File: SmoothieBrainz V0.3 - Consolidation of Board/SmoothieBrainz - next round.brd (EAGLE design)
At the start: 101 x 101 mm, 213 parts, among them IC1 LPC1769, IC5 LD117ADT33TR, Q1 BSL207SP, Q2 12MHz, SW1 SW_TACT_4P_B, SW3 SW_TACT_4P_B, U3 USD-SOCKETUSD, X1 MSTBA2, X14 USBPTH, X2 GMSTBA2, X3 GMSTBA4, X4 1751248, X5 1751248, X6 1751248, X7 1751248

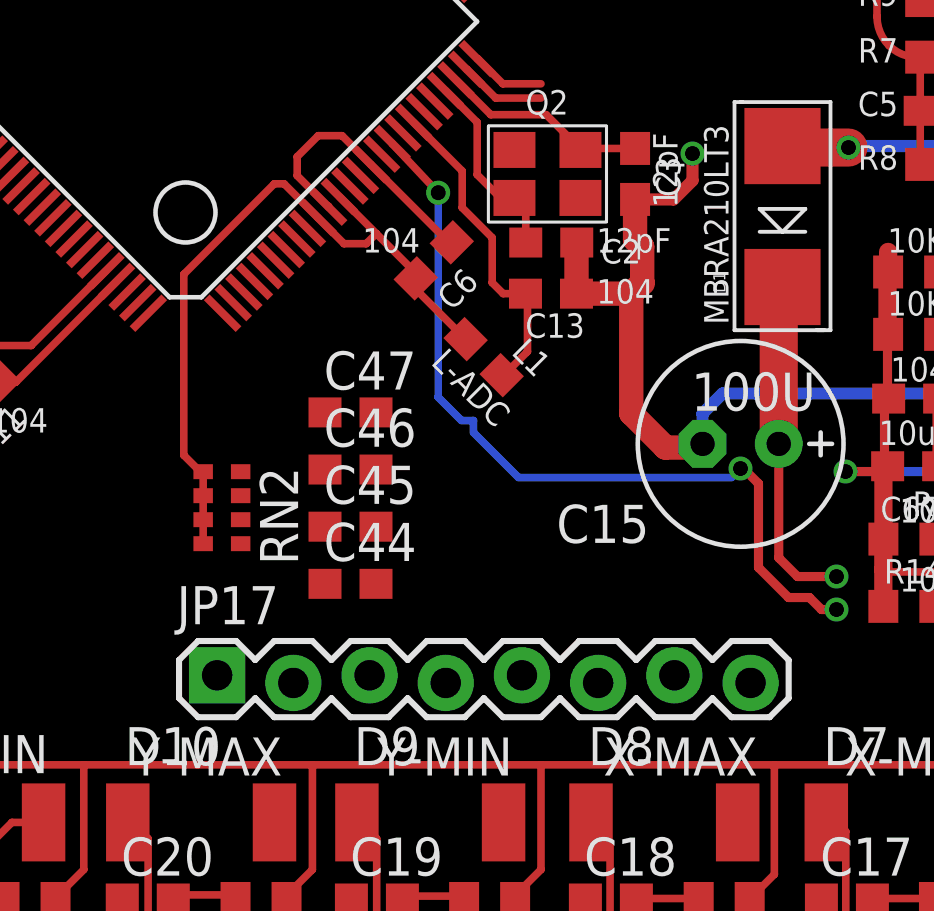
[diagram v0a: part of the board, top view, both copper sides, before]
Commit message: thermistor circuit, needs to be redone.  big time.
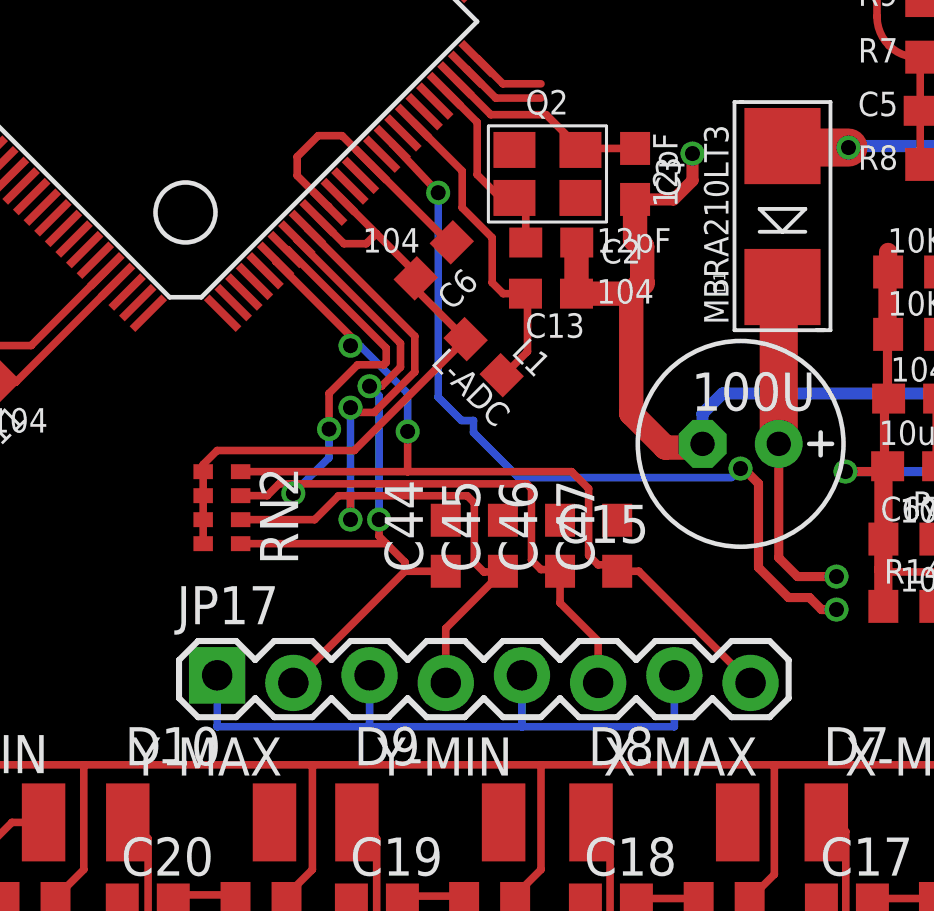
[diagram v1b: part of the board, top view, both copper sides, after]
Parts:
- moved C47 9.94 mm to (72.4, 18.4), turned to 90 degrees
- moved C46 7.43 mm to (70.5, 18.4), turned to 90 degrees
- moved C45 5.12 mm to (68.6, 18.4), turned to 90 degrees
- moved C44 3.42 mm to (66.7, 18.4), turned to 90 degrees
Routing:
- net TH4: track 0.00 -> 30.3 mm, vias 0 -> 2
- net TH1_HOTEND: track 0.00 -> 29.4 mm, vias 0 -> 2
- net TH3: track 0.00 -> 29.3 mm, vias 0 -> 2
- net TH2_BED: track 0.00 -> 25.1 mm, vias 0 -> 2
- net AGND: track 9.07 -> 31.2 mm
- net AVCC: track 26.0 -> 23.7 mm

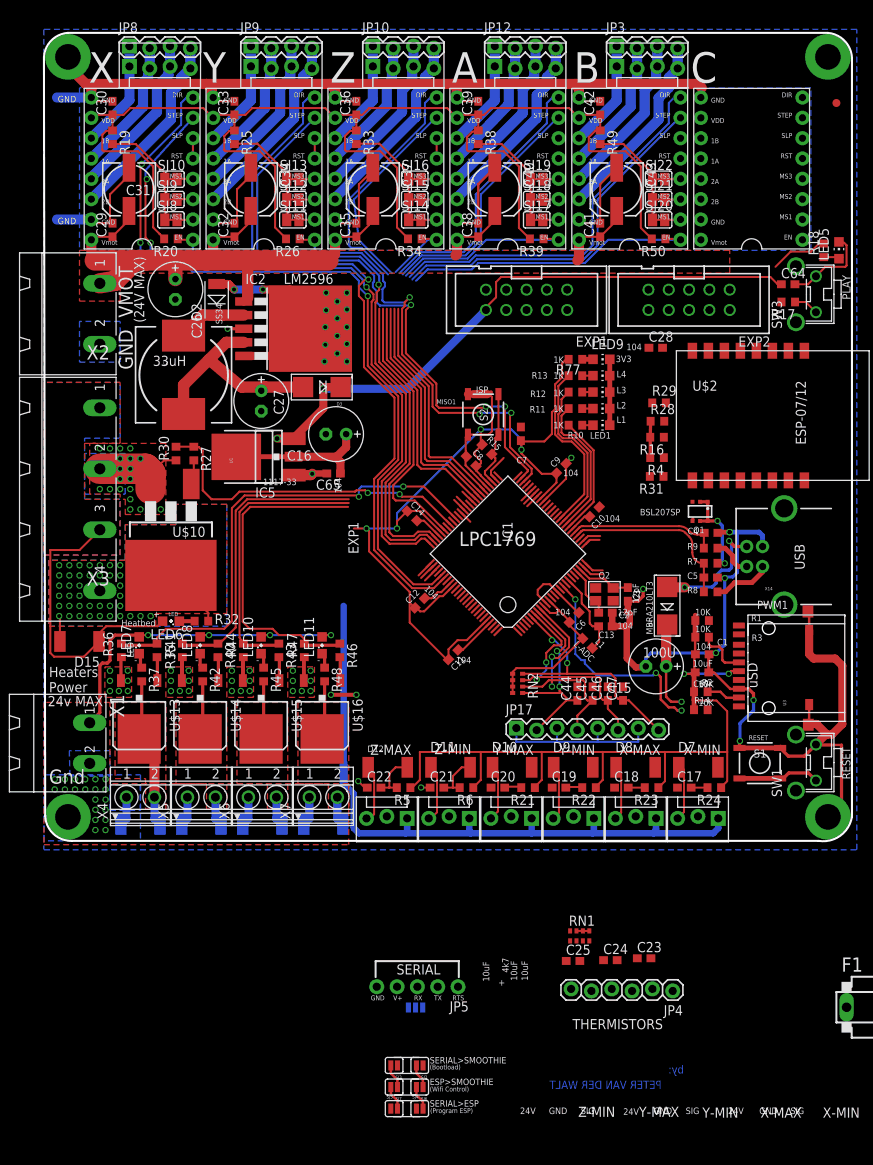
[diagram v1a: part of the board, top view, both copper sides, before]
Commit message: endstop power routing variant 1
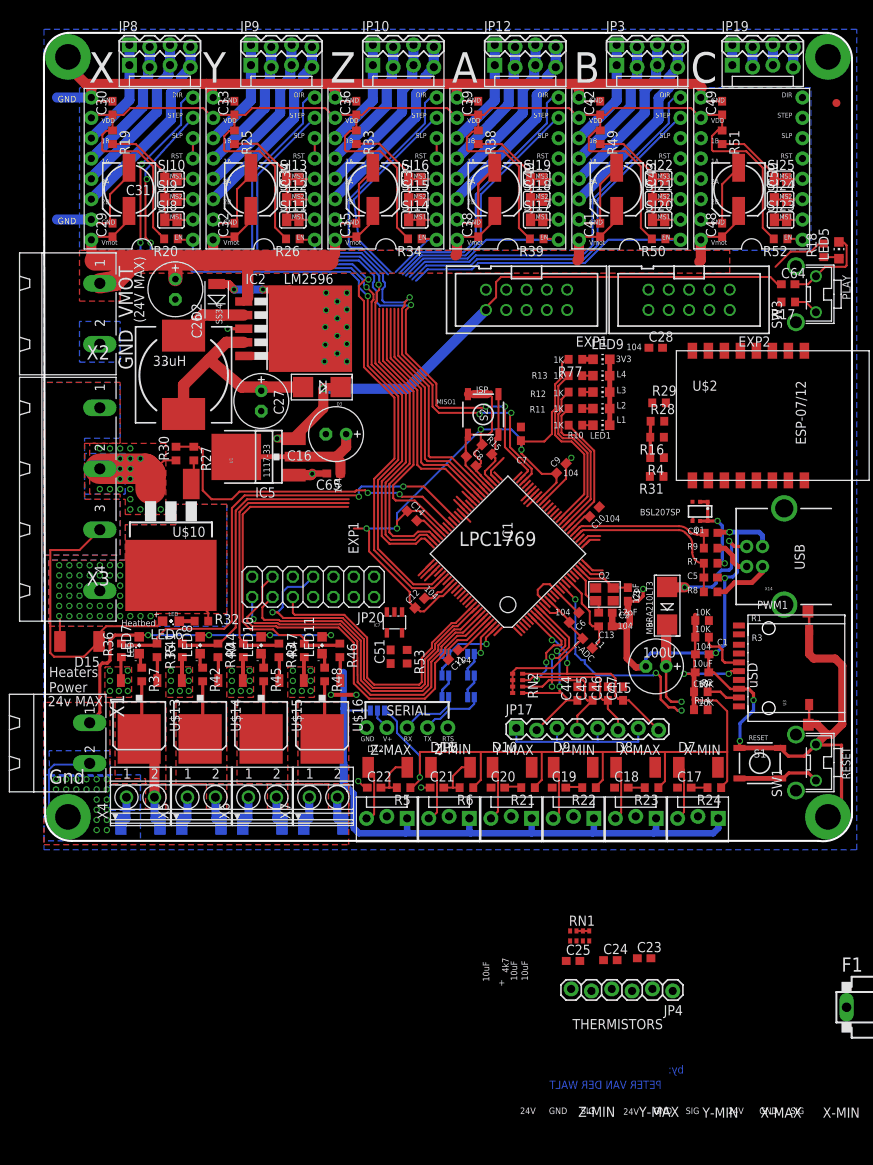
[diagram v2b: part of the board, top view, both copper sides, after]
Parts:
- added C48, C49: 104, resistor:C0603
- added C50: 100uF, resistor:153CLV-0605
- added C51: .1uF, resistor:C0603
- added IC7: (no value), microbuilder:SOT23-5
- added JP18: (no value), SparkFun-Connectors:MOLEX-1X4_LOCK
- added JP19: (no value), SparkFun-Connectors:1X04_LOCK
- added JP20: (no value), pinhead:2X07
- added R51: 1k, resistor:R0603
- added R52: 10k, resistor:R0603
- added R53: 22R, resistor:R0603
- added SJ23, SJ24, SJ25: (no value), jumper:SJ
- R1, R10, R11, R12, R13, R14, R15, R17, R18, R2, R3, R7, R77, R8, R9: device resistor:R0603@1 -> resistor:R0603
- moved SJ3 52.3 mm to (53.4, 23.4), flipped to the bottom
- moved SJ5 52.3 mm to (53.4, 18.0), flipped to the bottom
- moved SJ7 52.3 mm to (53.4, 20.7), flipped to the bottom
- moved SJ2 51.5 mm to (50.2, 23.4), flipped to the bottom
- moved SJ4 51.5 mm to (50.2, 18.0), flipped to the bottom
- moved SJ6 51.5 mm to (50.2, 20.7), flipped to the bottom
- moved SJ1 37.5 mm to (41.7, 16.3), turned to 0 degrees
- moved JP5 32.4 mm to (50.5, 14.2)
- moved JP1 0.16 mm to (71.6, 96.8)
- moved JP11 0.16 mm to (56.4, 96.8)
- moved JP2 0.16 mm to (25.9, 96.8)
- moved JP6 0.16 mm to (10.7, 96.8)
- moved JP7 0.16 mm to (41.1, 96.8)
- moved JP10 0.16 mm to (41.1, 99.4)
- moved JP12 0.16 mm to (56.4, 99.4)
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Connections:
- removed net VDD: U$9.VDD
- new net 1A$6M: JP18.2, JP19.2, U$9.1A
- new net 1B$6M: JP18.1, JP19.1, U$9.1B
- new net 2A$6M: JP18.3, JP19.3, U$9.2A
- new net 2B$6M: JP18.4, JP19.4, U$9.2B
- new net DIR6: U$9.DIR
- new net EN6: R52.1, U$9.EN
- new net N$48: U$9.RST, U$9.SLP
- new net N$49: R51.2, SJ23.1, SJ24.1, SJ25.1
- new net N$50: SJ23.2, U$9.MS1
- new net N$53: SJ24.2, U$9.MS2
- new net N$54: SJ25.2, U$9.MS3
- new net N$77: IC7.2, JP20.8
- new net N$78: IC7.4, R53.1
- new net STP6: U$9.STEP
- net 24V: now also C48.1, C50.+
- net 3.3V: now also C49.1, C51.1, IC7.5, JP20.1, JP20.2, R51.1, R52.2, U$9.VDD
- net ENET_CRS: now also JP20.7
- net ENET_MDC: now also JP20.5
- net ENET_MDIO: now also JP20.6
- net ENET_REF_CLK: now also R53.2
- net ENET_RXD0: now also JP20.10
- net ENET_RXD1: now also JP20.9
- net ENET_TXD0: now also JP20.11
- net ENET_TXD1: now also JP20.14
- net ENET_TX_EN: now also JP20.12
- net GND: now also C48.2, C49.2, C50.-, C51.2, IC7.3, JP20.3, JP20.4
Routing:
- net ENET_TXD0: track 0.00 -> 49.9 mm
- net ENET_CRS: track 0.00 -> 46.5 mm, vias 0 -> 1
- net ENET_TXD1: track 0.00 -> 44.7 mm, vias 0 -> 1
- net ENET_TX_EN: track 0.00 -> 43.1 mm
- net 3.3V: track 421.7 -> 461.2 mm, vias 6 -> 7
- net ENET_RXD0: track 0.00 -> 37.3 mm
- net GND: track 448.4 -> 475.1 mm
- net 24V: track 94.8 -> 104.5 mm
- net N$49: track 0.00 -> 8.82 mm
- net TX_FT: track 0.00 -> 8.00 mm
- net RX_0: track 3.04 -> 10.7 mm, vias 0 -> 1
- net RX_FT: track 0.00 -> 7.44 mm
- net TX_0: track 3.04 -> 7.89 mm, vias 0 -> 1
- net 5V: track 173.2 -> 168.3 mm
- net N$23: track 0.00 -> 2.64 mm
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
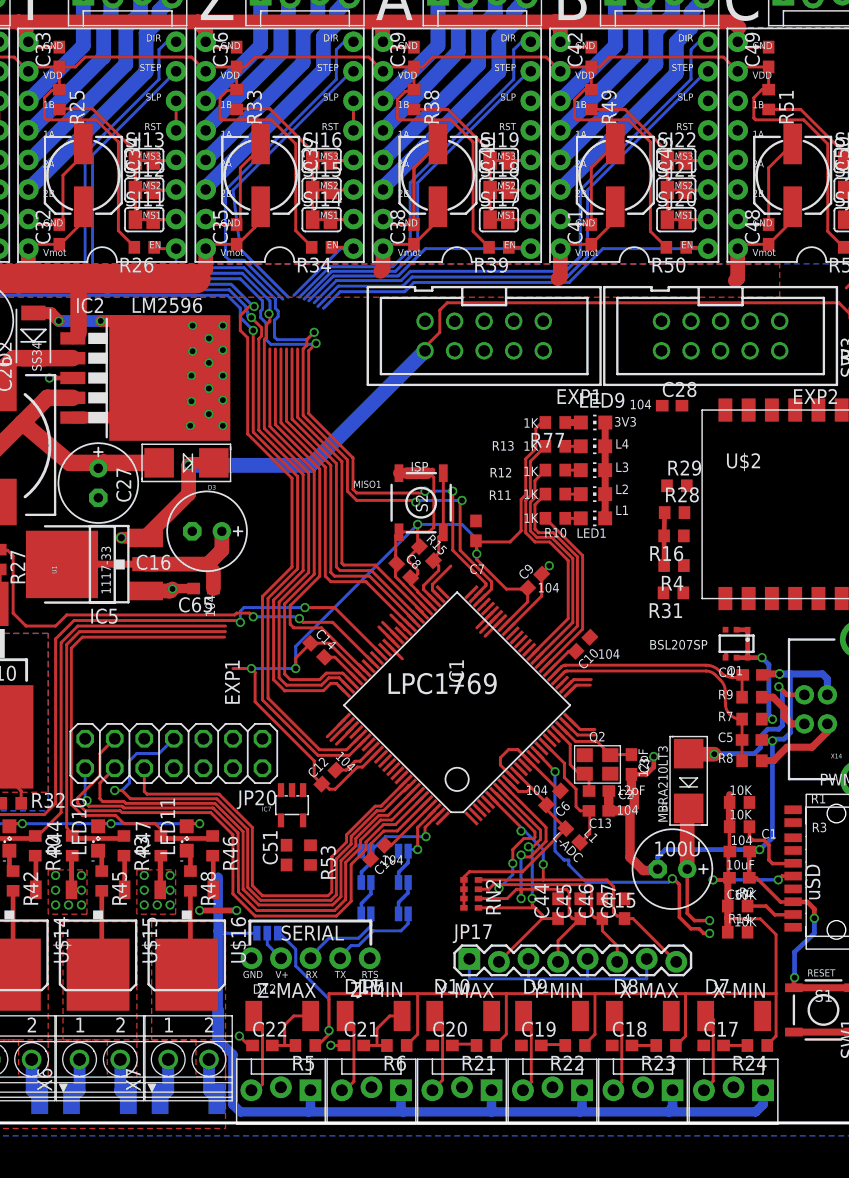
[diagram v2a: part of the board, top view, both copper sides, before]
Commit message: lots of motor routing complete
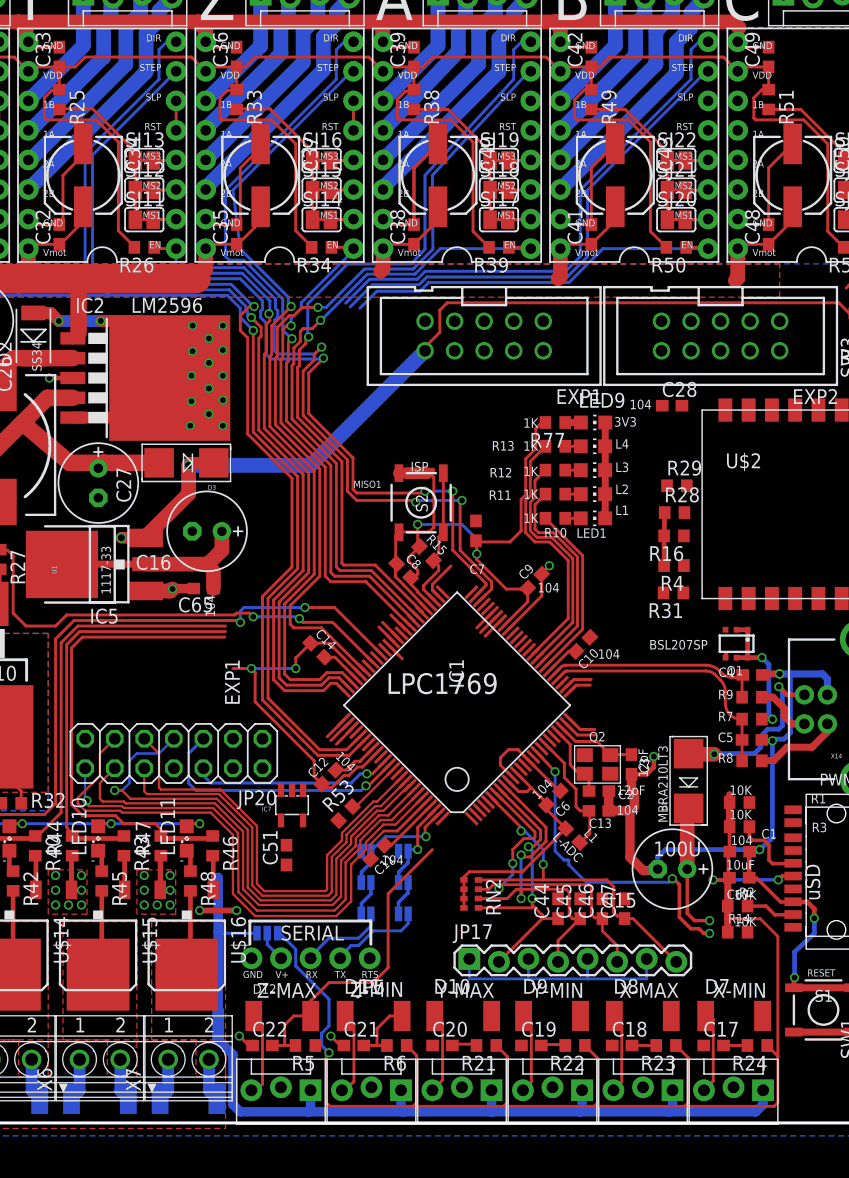
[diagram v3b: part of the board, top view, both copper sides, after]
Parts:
- moved R53 4.68 mm to (48.4, 26.6), turned to 45 degrees
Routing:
- net ENET_RXD1: track 0.00 -> 38.3 mm
- net ENET_MDC: track 0.00 -> 22.7 mm, vias 0 -> 1
- net Z_MAX: track 8.16 -> 29.0 mm
- net ENET_MDIO: track 0.00 -> 17.3 mm, vias 0 -> 1
- net STP4: track 65.3 -> 71.1 mm, vias 0 -> 1
- net STP3: track 62.7 -> 68.2 mm, vias 0 -> 1
- net EN3: track 38.8 -> 43.7 mm, vias 0 -> 1
- net ENET_REF_CLK: track 0.00 -> 4.88 mm
- net DIR3: track 59.6 -> 64.4 mm, vias 0 -> 1
- net DIR4: track 62.5 -> 67.0 mm, vias 0 -> 1
- net EN4: track 52.1 -> 55.7 mm, vias 0 -> 1
- net EN5: track 37.1 -> 34.0 mm
- net STP5: track 45.3 -> 42.5 mm
- net 3.3V: track 461.2 -> 458.5 mm
- net DIR5: track 48.0 -> 45.3 mm
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
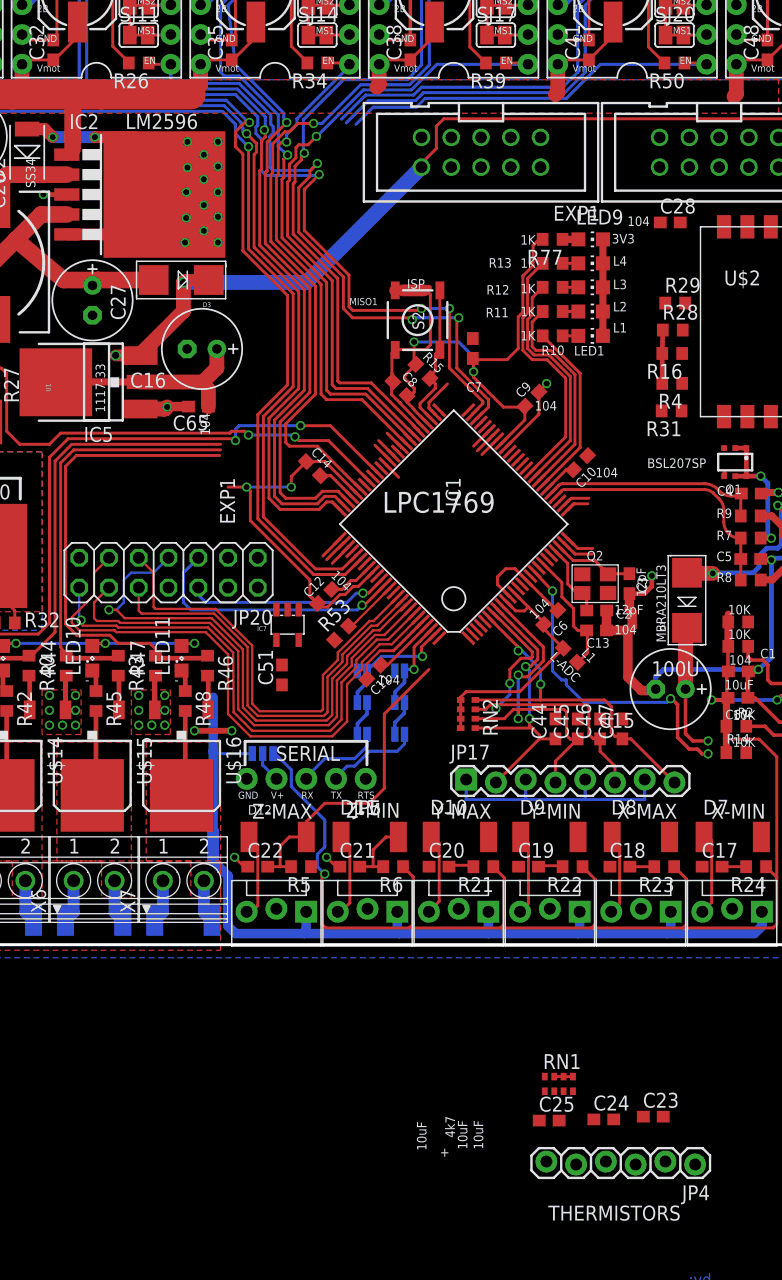
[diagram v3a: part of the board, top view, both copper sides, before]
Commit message: removed old thermistors
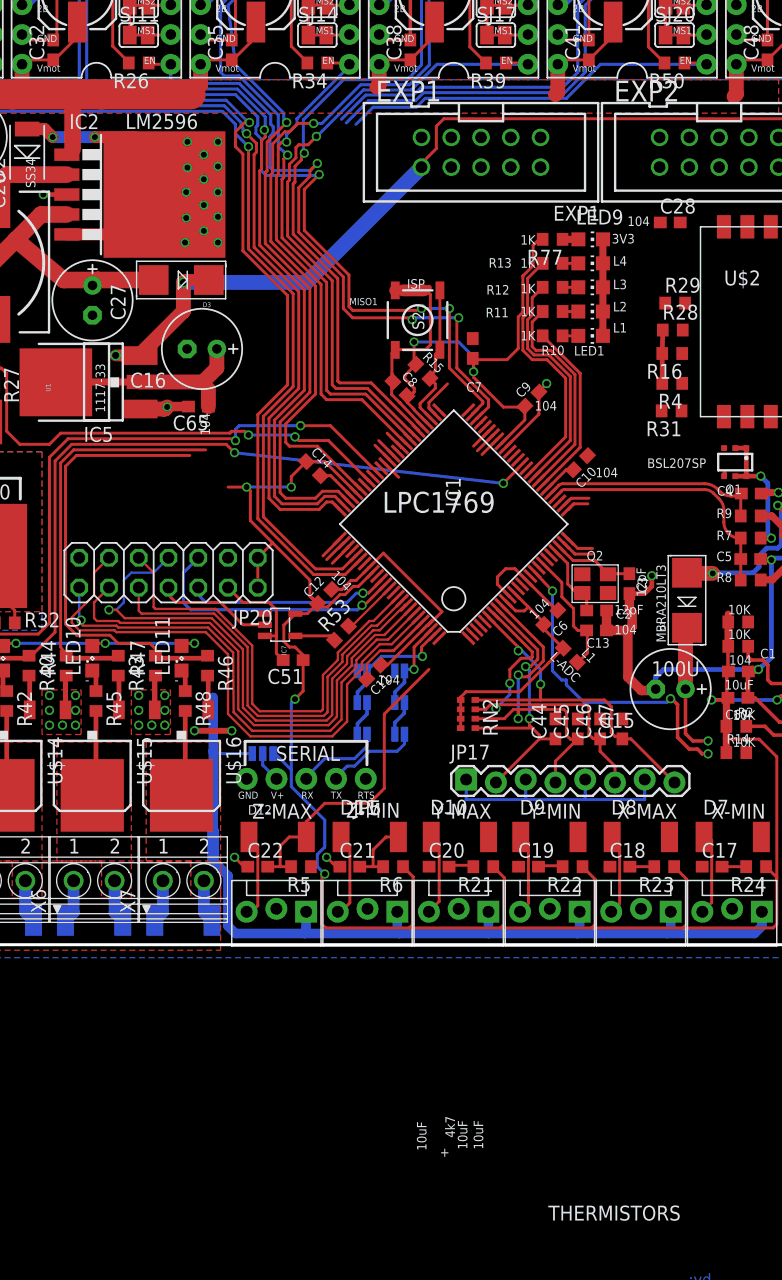
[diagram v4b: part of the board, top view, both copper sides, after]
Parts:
- removed C23, C24, C25: 10uF, resistor:C0603
- removed JP4: (no value), SparkFun-Connectors:1X06_LOCK
- removed RN1: 4.7K, resistor-dil:0603-ARV
- moved C51 1.59 mm to (44.3, 24.3), turned to 180 degrees
- moved IC7 0.63 mm to (43.2, 27.3), turned to 270 degrees
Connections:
- net AGND: no longer C23.2, C24.2, C25.2, JP4.1, JP4.3, JP4.5
- net AVCC: no longer RN1.1, RN1.2, RN1.3
- net TH1_HOTEND: no longer C23.1, JP4.2, RN1.8
- net TH2_BED: no longer C24.1, JP4.4, RN1.7
- net TH3: no longer C25.1, JP4.6, RN1.6
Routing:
- net P1_23-3RD-LARGE-FET: track 37.0 -> 63.4 mm, vias 0 -> 2
- net 3.3V: track 458.5 -> 480.2 mm, vias 7 -> 8
- net GND: track 475.2 -> 496.5 mm
- net N$77: track 0.00 -> 9.91 mm
- net N$78: track 0.00 -> 3.49 mm
- net P2.6_FAN_FET: track 40.8 -> 38.3 mm
- net AVCC: track 23.7 -> 22.1 mm
- net P1_22-3RD-SMALL-FET: track 35.4 -> 34.1 mm
